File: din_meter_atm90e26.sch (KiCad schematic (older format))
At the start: 49 parts, among them J1 USEL, J2 MMD1, J3 MMD0, J4 CONN_02X18, J5 CONN_01X10, J6 USEL, J7 MMD1, J8 MMD0, M1 ATM90E26_ATM90E26, M2 ATM90E26_ATM90E26, Y1 Crystal_Small, Y2 Crystal_Small

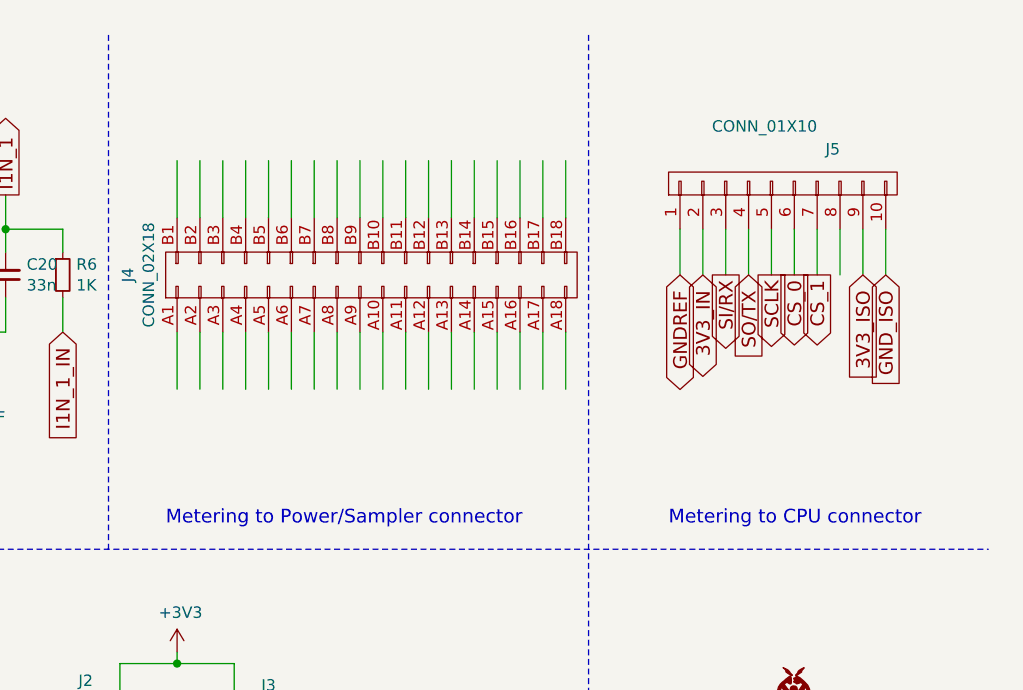
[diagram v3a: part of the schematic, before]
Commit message: Add labels to PCI-X
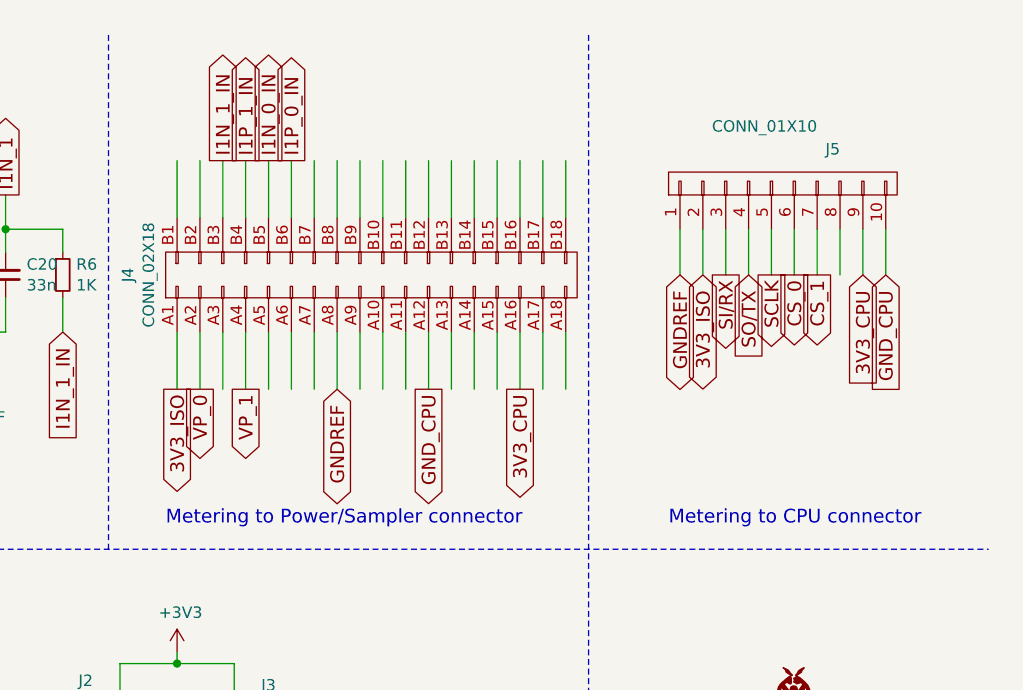
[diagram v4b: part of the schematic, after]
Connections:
- net labels added: 3V3_CPU, GND_CPU
- net labels removed: 3V3_IN, GND_ISO
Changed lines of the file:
@@
 $EndComp
 Text GLabel 10800 1500 3    60   Input ~ 0
-GND_ISO
+GND_CPU
 Text GLabel 10700 1500 3    60   Input ~ 0
+3V3_CPU
+Text GLabel 10000 1500 3    60   BiDi ~ 0
 3V3_ISO
-Text GLabel 10000 1500 3    60   BiDi ~ 0
-3V3_IN
 Text GLabel 9900 1500 3    60   BiDi ~ 0
 GNDREF
@@
 Text GLabel 5100 1100 1    60   Output ~ 0
 I2N_1
+Text GLabel 7700 2000 3    60   Output ~ 0
+3V3_ISO
+Text GLabel 7800 2000 3    60   Output ~ 0
+VP_0
+Text GLabel 8000 2000 3    60   Output ~ 0
+VP_1
+Text GLabel 8400 2000 3    60   BiDi ~ 0
+GNDREF
+Text GLabel 9200 2000 3    60   Output ~ 0
+3V3_CPU
+Text GLabel 8800 2000 3    60   Output ~ 0
+GND_CPU
+Text GLabel 8200 1000 1    60   Output ~ 0
+I1P_0_IN
+Text GLabel 8100 1000 1    60   Output ~ 0
+I1N_0_IN
+Text GLabel 8000 1000 1    60   Output ~ 0
+I1P_1_IN
+Text GLabel 7900 1000 1    60   Output ~ 0
+I1N_1_IN
 $EndSCHEMATC

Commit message: v0.1 prepped for fab
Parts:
- added CF1_0: CF1_0, Measurement_Points:Measurement_Point_Round-SMD-Pad_Small, symbol TEST_1P
- added CF1_1: CF1_1, Measurement_Points:Measurement_Point_Round-SMD-Pad_Small, symbol TEST_1P
- added CF2_0: CF2_0, Measurement_Points:Measurement_Point_Round-SMD-Pad_Small, symbol TEST_1P
- added CF2_1: CF2_1, Measurement_Points:Measurement_Point_Round-SMD-Pad_Small, symbol TEST_1P
- added IRQ_0: IRQ_0, Measurement_Points:Measurement_Point_Round-SMD-Pad_Small, symbol TEST_1P
- added IRQ_1: IRQ_1, Measurement_Points:Measurement_Point_Round-SMD-Pad_Small, symbol TEST_1P
- added L1: GND_SUP, Inductors_SMD:L_0402, symbol L_Core_Ferrite_Small
- added L2: 3V3_SUP, Inductors_SMD:L_0402, symbol L_Core_Ferrite_Small
- added WARN_0: WARN_0, Measurement_Points:Measurement_Point_Round-SMD-Pad_Small, symbol TEST_1P
- added WARN_1: WARN_1, Measurement_Points:Measurement_Point_Round-SMD-Pad_Small, symbol TEST_1P
- added ZX_0: ZX_0, Measurement_Points:Measurement_Point_Round-SMD-Pad_Small, symbol TEST_1P
- added ZX_1: ZX_1, Measurement_Points:Measurement_Point_Round-SMD-Pad_Small, symbol TEST_1P
- C13, C14, C7: value C_Small -> 20p
- C6: value C_Small -> 20p; manf# (none) -> 04025A200JAT2A
- C8: manf# (none) -> GRM155B11A333KA01D
- C9: manf# (none) -> GRM155R71C104KA88D
- J5: manf# (none) -> 52418-1010
- M2: manf# (none) -> ATM90E26-YU-B
- R1: manf# (none) -> CRCW04021K00FKED
- Y1: manf# (none) -> 5XFA08192123TF80Q3
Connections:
- net labels added: GND_ISO
- wire segments 227 -> 246

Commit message: Update BOM
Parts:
- C15: manf# (none) -> GRM155B11A333KA01D
- L1, L2: manf# (none) -> BLM15AG100SN1D
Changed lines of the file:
@@
 F 2 "Capacitors_SMD:C_0402" H 2800 1500 50  0001 C CNN
 F 3 "" H 2800 1500 50  0001 C CNN
+F 4 "GRM155B11A333KA01D" H 2800 1500 60  0001 C CNN "manf#"
 	1    2800 1500
 	-1   0    0    1
@@
 F 2 "Inductors_SMD:L_0402" H 2750 2450 50  0001 C CNN
 F 3 "" H 2750 2450 50  0001 C CNN
+F 4 "BLM15AG100SN1D" H 2750 2450 60  0001 C CNN "manf#"
 	1    2750 2450
 	0    1    1    0
@@
 F 2 "Inductors_SMD:L_0402" H 3350 2450 50  0001 C CNN
 F 3 "" H 3350 2450 50  0001 C CNN
+F 4 "BLM15AG100SN1D" H 3350 2450 60  0001 C CNN "manf#"
 	1    3350 2450
 	0    1    1    0

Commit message: Update BOM
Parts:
- C6: manf# 04025A200JAT2A -> GRM1555C1H200JA01D
- C8: manf# GRM155B11A333KA01D -> GRM188R61A106KE69D
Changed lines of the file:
@@
 F 2 "Capacitors_SMD:C_0402" H 750 1700 50  0001 C CNN
 F 3 "" H 750 1700 50  0001 C CNN
-F 4 "04025A200JAT2A" H 750 1700 60  0001 C CNN "manf#"
+F 4 "GRM1555C1H200JA01D" H 750 1700 60  0001 C CNN "manf#"
 	1    750  1700
 	-1   0    0    1
@@
 F 2 "Capacitors_SMD:C_0603" H 1950 4150 50  0001 C CNN
 F 3 "" H 1950 4150 50  0001 C CNN
-F 4 "GRM155B11A333KA01D" H 1950 4150 60  0001 C CNN "manf#"
+F 4 "GRM188R61A106KE69D" H 1950 4150 60  0001 C CNN "manf#"
 	1    1950 4150
 	-1   0    0    1

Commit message: Add back logos and bump version
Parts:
- SYM1: footprint (none) -> Whatnick_logo:Fsilk_HV
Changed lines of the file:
@@
 F 0 "SYM1" V 10310 4400 50  0001 C CNN
 F 1 "SYM_Flash_Small" V 10490 4400 50  0001 C CNN
-F 2 "" H 10400 4375 50  0001 C CNN
+F 2 "Whatnick_logo:Fsilk_HV" H 10400 4375 50  0001 C CNN
 F 3 "" H 10800 4300 50  0001 C CNN
 	1    10400 4400
